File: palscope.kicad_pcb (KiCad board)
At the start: 2 copper layers, 70 x 50 mm, 39 parts, among them J1 Conn_Coaxial, J2 Y, J3 Z, J4 X, J5 CVcc, J6 CGND, Q1 2N3906, Q2 2N3904, Q3 2N3906, Q4 2N3904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

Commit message: .
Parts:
- moved C3 71.9 mm to (101.6, 157.5)
- moved D2 69.7 mm to (104.1, 121.9)
- moved R10 69.7 mm to (106.7, 132.1)
- moved U2 69.7 mm to (96.5, 125.7)
- moved C2 69.7 mm to (124.5, 121.9)
- moved D1 69.7 mm to (101.6, 127.0)
- moved J2 69.7 mm to (116.8, 154.9)
- moved J3 69.7 mm to (127.0, 154.9)
- moved Q2 69.7 mm to (101.6, 144.8)
- moved Q4 69.7 mm to (109.2, 121.9)
- moved R4 69.7 mm to (101.6, 152.4)
- moved R5 69.7 mm to (104.1, 139.7)
- moved R6 69.7 mm to (106.7, 127.0)
- moved RV2 69.7 mm to (116.8, 137.2)
- moved RV3 69.7 mm to (116.8, 144.8)
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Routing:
- net GND: track 74.8 -> 114.4 mm
- net +9V: track 41.9 -> 73.7 mm
- net COMPOSITE_IN: track 34.3 -> 9.33 mm
- net Net-(R3-Pad2): track 0.00 -> 20.3 mm
- net Net-(R2-Pad2): track 0.00 -> 15.2 mm
- net Net-(C6-Pad1): track 0.00 -> 2.54 mm
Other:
- board text added: "X"

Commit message: .
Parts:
- moved C3 95.7 mm to (137.2, 68.6)
- moved J2 92.4 mm to (165.1, 76.2)
- moved R4 86.4 mm to (142.2, 76.2), turned to -90 degrees
- moved R10 83.3 mm to (157.5, 66.0), turned to 180 degrees
- moved J3 80.7 mm to (165.1, 83.8)
- moved Q2 77.8 mm to (149.9, 83.8), turned to 90 degrees
- moved R5 71.9 mm to (152.4, 86.4)
- moved C2 68.8 mm to (121.4, 53.2), turned to -90 degrees
- moved RV3 66.8 mm to (127.0, 78.7), turned to -90 degrees
- moved R6 63.1 mm to (154.9, 86.4)
- moved Q4 61.5 mm to (157.5, 83.8), turned to 90 degrees
- moved D1 59.3 mm to (142.2, 83.8), turned to 90 degrees
- moved D2 52.4 mm to (144.8, 88.9)
- moved U2 51.4 mm to (129.5, 86.4), turned to 0 degrees
- moved RV2 48.3 mm to (114.3, 88.9)
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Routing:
- net GND: track 114.4 -> 252.4 mm
- net +9V: track 73.7 -> 187.8 mm
- net Net-(C4-Pad2): track 0.00 -> 53.3 mm
- net Y: track 0.00 -> 50.8 mm
- net Z: track 0.00 -> 50.8 mm
- net Net-(C5-Pad2): track 0.00 -> 30.5 mm
- net Net-(RV1-Pad2): track 0.00 -> 27.9 mm
- net Net-(RV2-Pad2): track 0.00 -> 25.4 mm
- net Net-(C5-Pad1): track 0.00 -> 17.8 mm
- net Net-(D1-Pad2): track 0.00 -> 17.8 mm
- net X: track 0.00 -> 12.7 mm
- net Net-(R13-Pad1): track 0.00 -> 10.2 mm
- net COMPOSITE_IN: track 9.33 -> 17.0 mm
- net Net-(C1-Pad2): track 0.00 -> 5.08 mm
- net Net-(D1-Pad1): track 0.00 -> 5.08 mm
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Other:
- board text added: "+9V"
- board text added: "GND"
- board text added: "Y"
- board text added: "Z"

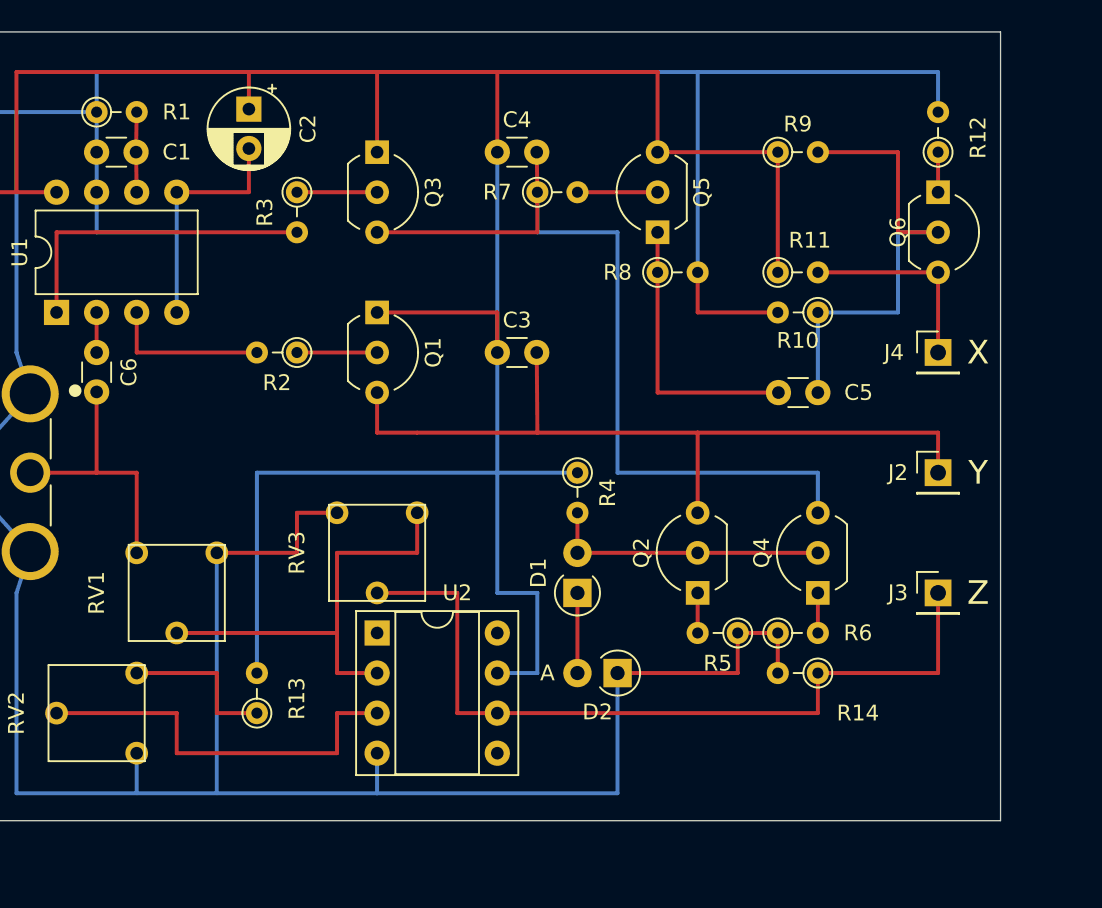
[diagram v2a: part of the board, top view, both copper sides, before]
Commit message: reworked PCB, removed useless connections, fixed bad C6 capacity
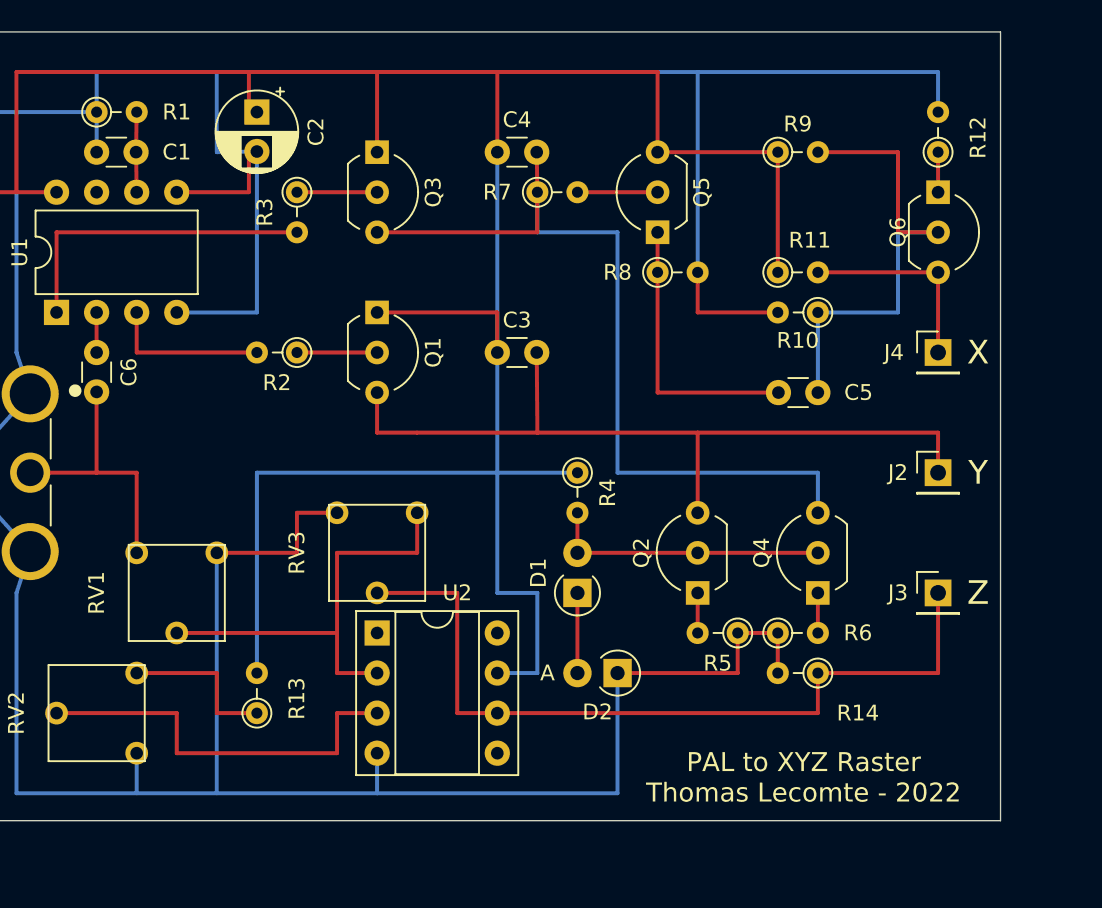
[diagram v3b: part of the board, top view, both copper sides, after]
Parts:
- C6: value 0.01n -> 0.01u
- moved C2 0.54 mm to (121.9, 53.3)
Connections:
- U1 pad 5: GND -> unconnected-(U1-Pad5)
- U1 pad 7: GND -> unconnected-(U1-Pad7)
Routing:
- net unconnected-(U1-Pad5): track 0.00 -> 7.34 mm
- net GND: track 252.4 -> 250.2 mm
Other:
- board text added: "PAL to XYZ Raster Thomas Lecomte - 2022"
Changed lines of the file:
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@@
   (net 26 "Net-(R3-Pad2)")
   (net 27 "Net-(R13-Pad1)")
+  (net 28 "unconnected-(U1-Pad5)")
+  (net 29 "unconnected-(U1-Pad7)")
   (footprint "Resistor_THT:R_Axial_DIN0204_L3.6mm_D1.6mm_P2.54mm_Vertical" (layer "F.Cu")
     (at 121.92 91.44 90)
@@
       (effects (font (size 1 1) (thickness 0.15)))
     )
-    (fp_text value "0.01n" (at 1.25 2.05 90) (layer "F.Fab")
+    (fp_text value "0.01u" (at 1.25 2.05 90) (layer "F.Fab")
       (effects (font (size 1 1) (thickness 0.15)))
     )
@@
       (net 1 "GND") (pinfunction "GND") (pintype "power_in"))
     (pad "5" thru_hole oval (at 7.62 7.62 90) (size 1.6 1.6) (drill 0.8) (layers *.Cu *.Mask)
-      (net 1 "GND") (pinfunction "BURST") (pintype "output"))
+      (net 28 "unconnected-(U1-Pad5)") (pinfunction "BURST") (pintype "output"))
     (pad "6" thru_hole oval (at 7.62 5.08 90) (size 1.6 1.6) (drill 0.8) (layers *.Cu *.Mask)
       (net 9 "Net-(C1-Pad2)") (pinfunction "INT") (pintype "input"))
     (pad "7" thru_hole oval (at 7.62 2.54 90) (size 1.6 1.6) (drill 0.8) (layers *.Cu *.Mask)
-      (net 1 "GND") (pinfunction "O/E") (pintype "output"))
+      (net 29 "unconnected-(U1-Pad7)") (pinfunction "O/E") (pintype "output"))
     (pad "8" thru_hole oval (at 7.62 0 90) (size 1.6 1.6) (drill 0.8) (layers *.Cu *.Mask)
       (net 2 "+9V") (pinfunction "VCC") (pintype "power_in"))
@@
   )
   (footprint "Capacitor_THT:CP_Radial_D5.0mm_P2.50mm" (layer "F.Cu")
-    (at 121.412 53.150888 -90)
+    (at 121.92 53.34 -90)
     (descr "CP, Radial series, Radial, pin pitch=2.50mm, , diameter=5mm, Electrolytic Capacitor")
     (tags "CP Radial series Radial pin pitch 2.50mm  diameter 5mm Electrolytic Capacitor")
@@
     (effects (font (size 1.5 1.5) (thickness 0.3)))
   )
+  (gr_text "PAL to XYZ Raster\nThomas Lecomte - 2022" (at 156.580614 95.523678) (layer "F.SilkS")
+    (effects (font (size 1.2 1.2) (thickness 0.2)))
+  )
   (gr_text "Z" (at 167.64 83.82) (layer "F.SilkS")
     (effects (font (size 1.5 1.5) (thickness 0.15)))
@@
     (effects (font (size 1.5 1.5) (thickness 0.15)))
   )
-  (segment (start 121.412 55.650888) (end 121.412 58.42) (width 0.25) (layer "F.Cu") (net 1))
   (segment (start 144.78 88.9) (end 152.4 88.9) (width 0.25) (layer "F.Cu") (net 1))
   (segment (start 152.4 88.9) (end 152.4 86.36) (width 0.25) (layer "F.Cu") (net 1))
   (segment (start 127 78.74) (end 124.46 78.74) (width 0.25) (layer "F.Cu") (net 1))
   (segment (start 154.94 86.36) (end 154.94 88.9) (width 0.25) (layer "F.Cu") (net 1))
-  (segment (start 121.412 58.42) (end 116.84 58.42) (width 0.25) (layer "F.Cu") (net 1))
   (segment (start 154.94 66.04) (end 149.86 66.04) (width 0.25) (layer "F.Cu") (net 1))
   (segment (start 124.46 78.74) (end 124.46 81.28) (width 0.25) (layer "F.Cu") (net 1))
@@
   (segment (start 106.68 83.82) (end 106.68 96.52) (width 0.25) (layer "B.Cu") (net 1))
   (segment (start 129.54 96.52) (end 144.78 96.52) (width 0.25) (layer "B.Cu") (net 1))
-  (segment (start 116.84 60.96) (end 111.76 60.96) (width 0.25) (layer "B.Cu") (net 1))
   (segment (start 165.1 50.8) (end 165.1 53.34) (width 0.25) (layer "B.Cu") (net 1))
   (segment (start 104.14 53.34) (end 106.68 53.34) (width 0.25) (layer "B.Cu") (net 1))
-  (segment (start 116.84 66.04) (end 116.84 60.96) (width 0.25) (layer "B.Cu") (net 1))
   (segment (start 106.68 53.34) (end 111.76 53.34) (width 0.25) (layer "B.Cu") (net 1))
   (segment (start 144.78 96.52) (end 144.78 88.9) (width 0.25) (layer "B.Cu") (net 1))
+  (segment (start 116.84 66.04) (end 121.92 66.04) (width 0.25) (layer "B.Cu") (net 1))
+  (segment (start 121.92 66.04) (end 121.92 55.84) (width 0.25) (layer "B.Cu") (net 1))
   (segment (start 107.55 81.2) (end 106.68 83.82) (width 0.25) (layer "B.Cu") (net 1))
   (segment (start 114.3 93.98) (end 114.3 96.52) (width 0.25) (layer "B.Cu") (net 1))
   (segment (start 106.68 96.52) (end 129.54 96.52) (width 0.25) (layer "B.Cu") (net 1))
-  (segment (start 116.84 58.42) (end 116.84 60.96) (width 0.25) (layer "B.Cu") (net 1))
   (segment (start 111.76 55.88) (end 111.76 53.34) (width 0.25) (layer "B.Cu") (net 1))
   (segment (start 149.86 63.5) (end 149.86 50.8) (width 0.25) (layer "B.Cu") (net 1))
@@
   (segment (start 111.76 50.8) (end 165.1 50.8) (width 0.25) (layer "B.Cu") (net 1))
   (segment (start 107.55 71.2) (end 106.68 68.58) (width 0.25) (layer "B.Cu") (net 1))
+  (segment (start 121.92 55.84) (end 119.38 55.88) (width 0.25) (layer "B.Cu") (net 1))
   (segment (start 103.05 76.2) (end 107.55 71.2) (width 0.25) (layer "B.Cu") (net 1))
   (segment (start 119.38 81.28) (end 119.38 96.52) (width 0.25) (layer "B.Cu") (net 1))
-  (segment (start 111.76 58.42) (end 111.76 55.88) (width 0.25) (layer "B.Cu") (net 1))
-  (segment (start 111.76 60.96) (end 111.76 58.42) (width 0.25) (layer "B.Cu") (net 1))
+  (segment (start 119.38 55.88) (end 119.38 50.8) (width 0.25) (layer "B.Cu") (net 1))
   (segment (start 106.68 58.42) (end 109.22 58.42) (width 0.25) (layer "F.Cu") (net 2))
   (segment (start 137.16 55.88) (end 137.16 50.8) (width 0.25) (layer "F.Cu") (net 2))
@@
   (segment (start 119.38 91.44) (end 119.38 88.9) (width 0.25) (layer "F.Cu") (net 27))
   (segment (start 119.38 88.9) (end 114.3 88.9) (width 0.25) (layer "F.Cu") (net 27))
+  (segment (start 121.412 55.650888) (end 121.412 58.42) (width 0.25) (layer "F.Cu") (net 28))
+  (segment (start 121.412 58.42) (end 116.84 58.42) (width 0.25) (layer "F.Cu") (net 28))
 )
